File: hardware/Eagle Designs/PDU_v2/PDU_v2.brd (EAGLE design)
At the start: 160 x 100 mm, 277 parts, among them J1 5037630291, J10 5037630691, J11 2PIN_HEADER, J12 2PIN_HEADER, J13 5037630291, J14 5037630291, J15 2PIN_HEADER, J16 5037630291, J17 5037630291, J18 5037630291, J19 5037630291, J2 5037630291, J20 503182-1852, J21 5037630491, J22 UJ31-CH-G1-SMT-TR, J23 2PIN_HEADER, J24 2PIN_HEADER, J25 2PIN_HEADER, J26 1729128, J27 5037630491, J28 5037630491, J3 5037630291, J4 5037630291, J5 5037630291, J6 5037630291, J7 5037630491, J8 5037630491, J9 5037630491, M1 BSZ100N06LS3, M2 BSZ100N06LS3, M3 BSZ033NE2LS5, M4 BSZ033NE2LS5, SW1 KMR231GLFS, T1 2N5088, U1 DRV8847PWPR, U10 PE014006, U11 IRLML2803PBFCT-ND, U12 IRLML2803PBFCT-ND, U13 LT8390EFE#PBF, U14 ATSAME51N19A-AF, U15 INA219BIDR, U16 MAX706RESA+T, U17 MAX16998AAUA+T, U18 ADT7311WTRZ, U19 NTGD1100LT1G, U2 DRV8847PWPR, U20 AO3400, U21 LT8609A, U22 LT8609A, U23 LT8609A, U3 LTC1477CS8LINEAR_TECHNOLOGY_L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, U4 LTC1477CS8LINEAR_TECHNOLOGY_L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, U5 LTC1477CS8LINEAR_TECHNOLOGY_L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, U6 LTC1477CS8LINEAR_TECHNOLOGY_L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, U7 LTC1477CS8LINEAR_TECHNOLOGY_L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, U8 LT8609A, U9 LTC1477CS8LINEAR_TECHNOLOGY_L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, Y1 ABS07-32.768KHZ-T

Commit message: updated PDU v2 (pre-routing)
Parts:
- removed C94: 1 uF, HSFL_Main_Library:0805
- removed C95, C97: 10 uF, HSFL_Main_Library:0805
- removed C96: 0.1 uF, HSFL_Main_Library:0805
- removed C98: 4.7 uF, HSFL_Main_Library:0805
- removed J11, J12, J15, J23, J24, J25: 2PIN_HEADER, HSFL_Main_Library:2MM_2PIN_HEADER
- removed R82: 10k, HSFL_Main_Library:0805
- removed R83: 40.2, HSFL_Main_Library:0805
- removed R86, R87, R90: 1k, HSFL_Main_Library:0805
- removed R88: 2.2 uH, Artemis:RESC0805X60N
- removed R89: 100, HSFL_Main_Library:0805
- removed T1: 2N5088, Artemis:TO92
- removed U$3, U$5: NDS8434, Artemis:SO08
- added J29: 61300411021, Artemis:CONN_61300411021_WRE
- added L7: 2.2 uH, Artemis:IND_BOURNS_SRP7030
- added Q1, Q2: FDS6375, Artemis:SOIC127P600X175-8N
- added R41: 84.5k, HSFL_Main_Library:0603-RES
- C24, C36: device HSFL_Main_Library:0805 -> HSFL_Main_Library:1210
- C30, C38, C54, C55, C56, C57, C58, C59, C60, C61, C62, C63, C64, C65, C66, C67, C68, C70, C71, C91: device HSFL_Main_Library:0805 -> HSFL_Main_Library:0603-CAP
- C37: value 10 nF -> 22 uF; device HSFL_Main_Library:0805 -> HSFL_Main_Library:0603-CAP
- C39: value 0.1 uF -> 33 pF; device HSFL_Main_Library:0805 -> HSFL_Main_Library:0603-CAP
- C40: value 4.7 uF -> 0.1 uF; device HSFL_Main_Library:0805 -> HSFL_Main_Library:0603-CAP
- C41: value 10 pF -> 1 uF; device HSFL_Main_Library:0805 -> HSFL_Main_Library:0603-CAP
- C42: value 22 uF -> 4.7 uF; device HSFL_Main_Library:1206 -> HSFL_Main_Library:0603-CAP
- C5: value 10 nF -> 0.01 uF
- C69: value 44 uF -> 22 uF; device HSFL_Main_Library:0805 -> HSFL_Main_Library:0603-CAP
- C89: value 4.7 uF -> 10 uF; device HSFL_Main_Library:0805 -> HSFL_Main_Library:0603-CAP
- C90: value 1 uF -> 4.7 uF; device HSFL_Main_Library:0805 -> HSFL_Main_Library:0603-CAP
- C92: value 33 pF -> 10 uF; device HSFL_Main_Library:0805 -> HSFL_Main_Library:0603-CAP
- C93: value 0 uF -> 1 uF; device HSFL_Main_Library:0805 -> HSFL_Main_Library:0603-CAP
- J18, J19: value 5037630291 -> 5037630491; device Artemis:CON_5037630291 -> Artemis:CON_5037630491
- J22: value UJ31-CH-G1-SMT-TR -> UJ31-CH-314-SMT-TR; device Artemis:CUI_UJ31-CH-G1-SMT-TR -> Artemis:CUI_UJ31-CH-314-SMT-TR
- J27, J28: value 5037630491 -> 5037630691; device Artemis:CON_5037630491 -> Artemis:CONN_503763-0691_MOL
- L1, L3: device Artemis:IND_XFL4020-222ME -> Artemis:IND_BOURNS_SRP7030
- L2: value 1 uH -> 1 uH; device HSFL_Main_Library:ELL4GG -> Artemis:INDC1608X95N
- L4: value 2.2 uH -> 10 uH; device Artemis:IND_XFL4020-222ME -> Artemis:INDC2012X100N
- L6: value 10uH -> 2.2 uH; device HSFL_Main_Library:XFL4030472MEB -> Artemis:IND_BOURNS_SRP7030
- NT1, NT2, NT3: value 0 H -> AIMC-0805-2N2S-T; device HSFL_Main_Library:ELL4GG -> Artemis:INDC2012X105N
- R15: value 300k -> 301k
- R16, R24: value 49.9k -> 47k
- R23: value 182k -> 180k
- R26: value 18.2 K -> 1k; device HSFL_Main_Library:0805 -> HSFL_Main_Library:0603-RES
- R27: value 187 K -> 100; device HSFL_Main_Library:0805 -> HSFL_Main_Library:0603-RES
- R28: value 100 K -> 10k; device HSFL_Main_Library:0805 -> HSFL_Main_Library:0603-RES
- R29: value 1 M -> 40.2k; device HSFL_Main_Library:0805 -> HSFL_Main_Library:0603-RES
- R37: value 10 uH -> 2k; device Artemis:RESC0805X60N -> HSFL_Main_Library:0603-RES
- R38, R39, R40, R42, R45, R48, R49, R50, R51, R52, R53, R54, R55, R56, R64, R67, R72, R73, R74, R75, R76, R77, R78: device HSFL_Main_Library:0805 -> HSFL_Main_Library:0603-RES
- R59: value 80k -> 100k
- R60: value 50k -> 62k
- R63: value 125k -> 130k
- R65: value 191k -> 180k
- R66: value 9k -> 9.09k; device HSFL_Main_Library:0805 -> HSFL_Main_Library:0603-RES
- R79: value 71.5k -> 68.1k; device HSFL_Main_Library:0805 -> HSFL_Main_Library:0603-RES
- R80: value 86.6k -> 1k; device HSFL_Main_Library:0805 -> HSFL_Main_Library:0603-RES
- R81: value 2k -> 1k; device HSFL_Main_Library:0805 -> HSFL_Main_Library:0603-RES
- U20: value AO3400 -> AO3404A
- U23: value LT8609A -> BC848ALT1G; device HSFL_Main_Library:MSOP-10_MSE -> Artemis:SOT-23_ONS
- Y1: value ABS07-32.768KHZ-T -> CC4V-T1A-32.768KHZ-12.5PF-20PPM-TA-QC; device Artemis:XTAL_ABS07-32.768KHZ-T -> Artemis:XTAL_CC4V-T1A-32.768KHZ-12.5PF-20PPM-TA-QC
- moved R45 618.4 mm to (-520.7, -193.0)
- moved R50 596.1 mm to (-516.9, -193.0)
- moved L6 595.4 mm to (-518.2, -218.4)
- moved R51 586.5 mm to (-509.3, -193.0)
- moved R52 585.6 mm to (-513.1, -193.0)
- moved C30 582.3 mm to (-501.6, -193.0)
- moved R53 576.1 mm to (-505.5, -193.0)
- moved C66 574.1 mm to (-496.6, -193.0)
- moved C68 562.7 mm to (-491.5, -193.0)
- moved C67 555.3 mm to (-476.2, -193.0)
- moved C69 551.6 mm to (-481.3, -193.0)
- moved C37 548.1 mm to (-486.4, -193.0)
- moved C70 540.6 mm to (-471.2, -193.0)
- moved R57 531.0 mm to (-466.1, -189.2)
- moved R58 530.3 mm to (-466.1, -193.0)
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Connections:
- removed net 5V_BURN_RELAY: U14.54
- removed net BURNWIREHERE________________________: H1.2.8
- removed net N$33: C38.1, U23.3
- removed net N$34: C39.1, U23.1
- removed net N$35: C39.2, L4.1, U23.2
- removed net N$36: C41.1, R27.2, R29.1, U23.6
- removed net N$72: CR1.2, J11.1
- removed net N$73: CR2.2, J12.1
- removed net N$74: R89.2, R90.2, U20.3
- removed net N$75: CR3.2, J15.1
- removed net N$78: CR4.2, J23.1
- removed net N$79: CR5.2, J24.1
- removed net N$80: CR6.2, J25.1
- removed net N$98: NT1.P$2, R89.1, U$1.12
- removed net PG_5V_BURN: R28.1, U23.8
- removed net SOLAR_VS: C29.1, R34.1, R36.1, U15.5
- removed net SW_5V_BURN: C41.2, C42.1, L4.2, R28.2, R29.2
- removed net SW_5V_BURN_EN: U23.10
- removed net UART_TXD: H1.1.2
- new net BUS_3V1: L3.1
- new net N$20: L3.2
- net +3V3: now also R54.2, R58.2; no longer R54.1, R58.1
- net 12V_SW1: now also J10.5, L6.1; no longer J10.3, L6.2
- net 5V_BURN: now also H1.2.8, U14.54, U23.1; no longer T1.2
- net BATT_CHRG: now also C92.2, C93.2, J29.4; no longer C94.2, C95.2
- net BATT_CHRG_DISP: now also R40.2; no longer R40.1
- net BC_VCC: now also R37.1; no longer R81.1
- net BUS_3V3: now also C29.1, L1.1, R34.1, R36.1, U15.5; no longer L1.2
- net BUS_5V: no longer L3.2
- net GND: now also C37.1, C42.1, C69.1, C72.1, C90.1, C92.1, C93.1, J10.2, J18.2, J18.5, J18.6, J19.2, J19.5, J19.6, J22.SH10, J22.SH7, J22.SH8, J22.SH9, J27.2, J27.4, J28.2, J9.2, NT1.1, NT2.1, NT3.1, R40.1, U23.2; no longer C37.2, C38.2, C40.2, C42.2, C56.1, C57.1, C58.1, C59.1, C60.1, C69.2, C72.2, C94.1, C95.1, C97.1, C98.1, J10.5, J11.2, J12.2, J15.2, J18.3, J19.3, J23.2, J24.2, J25.2, J27.5, J28.5, J28.6, J9.3, NT1.P$1, NT2.P$1, NT3.P$1, R27.1, R38.1, R40.2, R90.1, T1.3, U14.12, U14.25, U14.30, U14.39, U14.51, U14.63, U14.77, U14.92, U23.11, U23.5
- net GNDA: now also C38.1, C39.1, C40.2, C41.2, NT1.2, NT2.2, R29.1, R41.2; no longer C90.2, C91.2, C92.1, C93.1, NT2.P$2, NT3.P$2, R83.1, R86.2
- net INH_SW1_COM: now also J18.3; no longer J18.2
- net INH_SW3_COM: now also J19.3; no longer J19.2
- net LX: now also L7.1; no longer R88.2
- net MID: now also NT3.2, R27.1, U$1.12
- net MOSI: now also J27.3; no longer J27.2
- net N$100: now also C91.2; no longer C96.2
- net N$12: now also L1.2; no longer L1.1
- net N$13: now also Q1.1, Q1.2, Q1.3, Q2.1, Q2.2, Q2.3; no longer U$3.1, U$3.2, U$3.3, U$5.1, U$5.2, U$5.3
- net N$15: now also Q2.4; no longer U$5.4
- net N$16: now also U23.3; no longer T1.1
- net N$18: now also Q1.4; no longer U$3.4
- net N$29: no longer L3.1
- net N$31: now also R27.2, U20.3; no longer U23.4
- net N$32: now also C56.1, C57.1, C58.1, C59.1, C60.1, R38.1, U14.12, U14.25, U14.30, U14.39, U14.51, U14.63, U14.77, U14.92; no longer C37.1, U23.7
- net N$43: now also L2.1; no longer L2.P$1
- net N$46: now also L4.2; no longer R37.2
- net N$51: now also L2.2; no longer L2.P$2
- net N$58: now also L4.1; no longer R37.1
- net N$66: now also C72.2; no longer C72.1
- net N$87: now also C41.1; no longer C90.1
- net N$89: now also R41.1; no longer R80.1
- net N$90: now also C40.1; no longer C91.1
- net N$92: now also R37.2; no longer R81.2
- net N$93: now also R28.2, R29.2; no longer R82.2, R83.2
- net N$95: now also C39.2, R28.1; no longer C92.2, R82.1
- net N$97: now also C38.2; no longer C93.2
- net N$99: now also R80.1, R81.1; no longer R86.1, R87.1
- net PB16: now also J28.3; no longer J28.1
- net PB17: now also J28.1; no longer J27.4
- net PB22: now also J28.6; no longer J28.3
- net PB23: now also J28.5; no longer J28.2
- net RESET: now also R58.1; no longer R58.2
- net SCK: now also J27.5; no longer J27.3
- net SOLAR_IN1: now also CR1.2, R35.1, U15.8
- net SOLAR_IN2: now also CR2.2
- net SOLAR_IN3: now also CR3.2
- net SOLAR_IN4: now also CR4.2
- net SOLAR_IN5: now also CR5.2
- net SOLAR_IN6: now also CR6.2
- net SW: now also C91.1, L7.2; no longer C96.1, R88.1
- net SWCLK: now also R54.1; no longer R54.2
- net SW_3V3_BUS: now also L6.2; no longer L6.1
- net SW_5V_1: now also J10.3; no longer J10.2
- net SW_5V_2: now also J26.1
- net SW_5V_3: now also J9.3; no longer J26.1, J9.2
- net UART2_TXD: now also H1.1.2
- net USB_JUMP1: now also C37.2, C69.2, J29.1; no longer C69.1
- net USB_JUMP_BAT: now also J29.3
- net VBATT: now also J29.2, R81.2; no longer C40.1, R35.1, R87.2, U15.8, U23.9
- net VBURN1: now also Q1.5, Q1.6, Q1.7, Q1.8; no longer U$3.5, U$3.6, U$3.7, U$3.8
- net VBURN2: now also Q2.5, Q2.6, Q2.7, Q2.8; no longer U$5.5, U$5.6, U$5.7, U$5.8
- net VL: now also C42.2, C90.2; no longer C97.2, C98.2

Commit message: updated PDU v2 and Artemis Library
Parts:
- removed D1: (no value), Artemis:POWERDI-123
- removed U10: PE014006, Artemis:RELAY5-PE_CO
- added Q3: AO4485, Artemis:SOIC127P600X175-8N
- added R86: 10k, HSFL_Main_Library:0603-RES
- Q1, Q2: device Artemis:SOIC127P600X175-8N -> Artemis:SOIC127P600X175-8N@1
- R36: device HSFL_Main_Library:0603-RES -> HSFL_Main_Library:0805
- moved R45 660.7 mm to (83.8, 73.7), flipped to the bottom, turned to 180 degrees
- moved R50 653.2 mm to (83.8, 63.5), flipped to the bottom, turned to 270 degrees
- moved R51 648.9 mm to (85.1, 67.3), flipped to the bottom
- moved R52 647.4 mm to (81.3, 63.5), flipped to the bottom, turned to 90 degrees
- moved R53 638.0 mm to (78.7, 63.5), flipped to the bottom, turned to 90 degrees
- moved C30 632.2 mm to (76.2, 63.5), flipped to the bottom, turned to 270 degrees
- moved C66 625.3 mm to (73.7, 63.5), flipped to the bottom, turned to 270 degrees
- moved C68 615.9 mm to (67.3, 66.0), flipped to the bottom
- moved C70 613.4 mm to (80.0, 76.2), flipped to the bottom, turned to 90 degrees
- moved L6 613.2 mm to (44.5, 25.4), turned to 180 degrees
- moved C37 612.4 mm to (67.3, 68.6), flipped to the bottom, turned to 180 degrees
- moved L7 611.8 mm to (34.3, 63.5), turned to 270 degrees
- moved C67 610.0 mm to (71.1, 76.2), flipped to the bottom
- moved C69 608.9 mm to (67.3, 71.1), flipped to the bottom, turned to 180 degrees
- moved J29 602.8 mm to (14.0, 69.8), flipped to the bottom, turned to 90 degrees
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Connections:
- net N$100 renamed BST
- net N$31 renamed R26_R27
- net N$69 renamed BUS_EN_VIN
- net N$85 renamed ACOK
- net N$87 renamed BATT_CHRG_VCC
- net N$88 renamed ILIM
- net N$89 renamed ISET
- net N$90 renamed TMR
- net N$91 renamed CHGOK
- net N$93 renamed IB
- net N$94 renamed VNTC
- net N$95 renamed R28_C39
- net N$96 renamed NTC
- net N$97 renamed R85_C38
- net N$99 renamed FB
- removed net +3V3: C64.1, D2.3, J20.4, J21.1, R38.2, R42.2, R54.2, R55.2, R58.2, R60.2, R61.2, R62.2, U16.2
- removed net BUS_3V1: L3.1
- removed net N$20: L3.2
- net BUS_3V3: now also C64.1, D2.3, J20.4, J21.1, R38.2, R42.2, R54.2, R55.2, R58.2, R60.2, R61.2, R62.2, U16.2
- net BUS_5V: now also L3.1
- net GND: no longer U10.12
- net N$13: now also Q3.5, Q3.6, Q3.7, Q3.8; no longer U10.11
- net N$16: now also Q3.4, R86.1; no longer D1.A, U10.5
- net N$29: now also L3.2
- net PB16: now also J28.1; no longer J28.3
- net PB17: now also J28.3; no longer J28.1
- net PB22: now also J28.5; no longer J28.6
- net PB23: now also J28.6; no longer J28.5
- net VBATT: now also Q3.1, Q3.2, Q3.3, R86.2; no longer D1.C, U10.1, U10.14
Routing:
- net N$32: track 0.00 -> 50.3 mm, vias 0 -> 3
- net N$13: track 0.00 -> 45.5 mm, vias 0 -> 2
- net N$18: track 0.00 -> 33.8 mm
- net PB23: track 0.00 -> 29.0 mm
- net PB22: track 0.00 -> 28.8 mm
- net PB16: track 0.00 -> 28.6 mm
- net GND: track 0.00 -> 28.3 mm
- net PB17: track 0.00 -> 28.3 mm
- net VBURN2: track 0.00 -> 22.5 mm
- net WDT_WDI: track 0.00 -> 20.6 mm
- net VBURN1: track 0.00 -> 20.3 mm
- net N$23: track 0.00 -> 19.2 mm, vias 0 -> 2
- net N$21: track 0.00 -> 19.2 mm, vias 0 -> 2
- net N$54: track 0.00 -> 18.3 mm
- net VBATT: track 0.00 -> 18.2 mm, vias 0 -> 1
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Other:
- board size 160 x 100 mm -> 90.2 x 95.5 mm

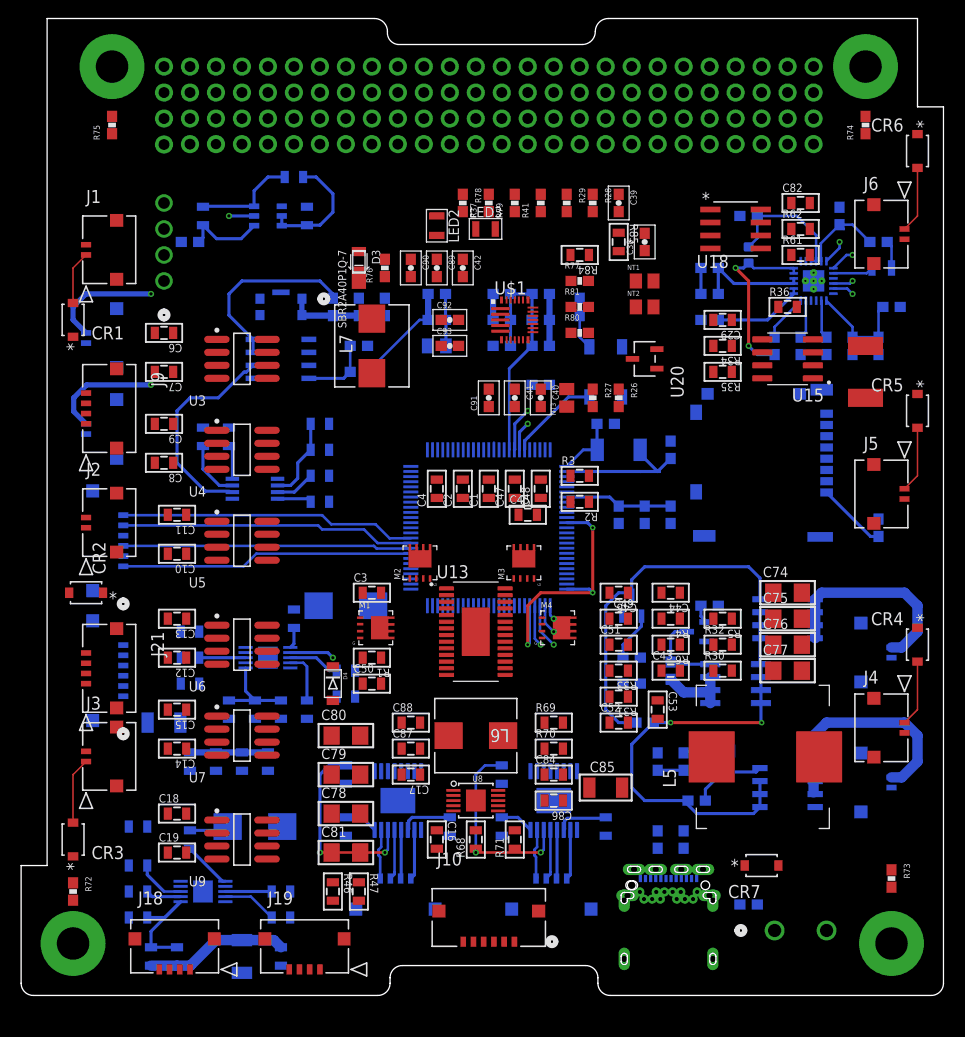
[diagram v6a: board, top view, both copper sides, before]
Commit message: updated PDU v2 (Routing Rough Draft complete)
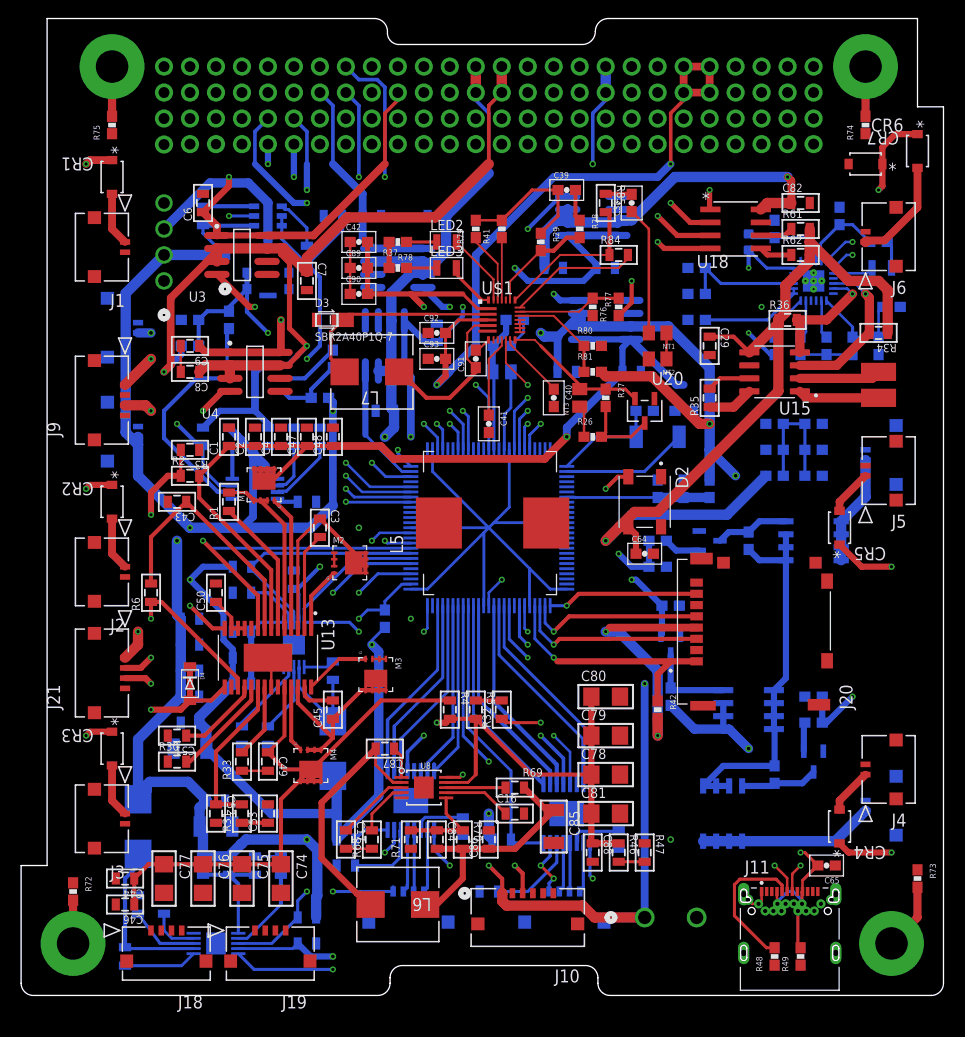
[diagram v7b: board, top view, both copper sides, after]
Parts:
- removed J22: UJ31-CH-314-SMT-TR, Artemis:CUI_UJ31-CH-314-SMT-TR
- removed J27, J28: 5037630691, Artemis:CONN_503763-0691_MOL
- added J11: UJ31-CH-G1-SMT-TR, Artemis:CUI_UJ31-CH-G1-SMT-TR
- moved CR7 69.3 mm to (82.5, 81.3), turned to 180 degrees
- moved C19 64.7 mm to (59.7, 61.0), flipped to the bottom, turned to 180 degrees
- moved C77 64.3 mm to (14.0, 11.4), turned to 270 degrees
- moved U9 62.0 mm to (57.1, 66.0), flipped to the bottom, turned to 180 degrees
- moved C76 61.6 mm to (17.8, 11.4), turned to 270 degrees
- moved U7 61.3 mm to (55.9, 76.2), flipped to the bottom, turned to 180 degrees
- moved C44 60.2 mm to (10.2, 11.4)
- moved C15 60.2 mm to (57.1, 71.1), flipped to the bottom
- moved C14 59.7 mm to (52.1, 71.1), flipped to the bottom
- moved C75 59.1 mm to (21.6, 11.4), turned to 270 degrees
- moved C18 57.6 mm to (53.3, 61.0), flipped to the bottom, turned to 180 degrees
- moved C46 57.1 mm to (10.2, 8.89)
- moved C74 56.9 mm to (25.4, 11.4), turned to 270 degrees
- moved R30 54.1 mm to (15.2, 22.9)
- moved R6 51.1 mm to (12.7, 39.4), turned to 90 degrees
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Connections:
- net N$32 renamed VDD
- removed net +3V3_BUS: R43.1, R44.1
- removed net +5V_BUS: C25.2, C26.2, C27.2, C28.2, U1.12, U2.12
- removed net MISO: J27.1, U14.48
- removed net MOSI: J27.3, U14.46
- removed net N$42: U13.23
- removed net N$65: D2.2, U14.95
- removed net PB16: J28.1, U14.58
- removed net PB17: J28.3, U14.59
- removed net PB22: J28.5, U14.60
- removed net PB23: J28.6, U14.61
- removed net PDU_RX: H1.1.51, U14.83
- removed net PDU_TX: H1.1.49, U14.82
- removed net SCK: J27.5, U14.47
- new net LED: D2.2, U14.73
- new net N$20: H1.1.32
- net 5V_BURN: now also U14.82; no longer H1.2.8, U14.54
- net 5V_USB_CHRG: no longer H1.1.32
- net BURN1_EN: now also U14.83; no longer U14.55
- net BURN2_EN: now also U14.84; no longer U14.70
- net BUS_3V3: now also R43.1, R44.1
- net BUS_3V3_PG: now also U14.58; no longer U14.71
- net BUS_5V: now also C25.2, C26.2, C27.2, C28.2, U1.12, U2.12
- net BUS_5V_PG: now also U14.56; no longer U14.75
- net BUS_EN: now also U14.57; no longer U14.74
- net CUS_SCL: now also U14.93; no longer U14.73
- net CUS_SDA: now also U14.94; no longer U14.72
- net FAULT1: now also U14.42; no longer H1.1.40, U14.65
- net FAULT2: no longer H1.1.46, U14.80
- net GND: now also J11.A1, J11.A12, J11.B1, J11.B12, J11.SH1, J11.SH2, J11.SH3, J11.SH4, J11.SH5, J11.SH6; no longer J22.A1, J22.A12, J22.B1, J22.B12, J22.SH1, J22.SH10, J22.SH2, J22.SH3, J22.SH4, J22.SH5, J22.SH6, J22.SH7, J22.SH8, J22.SH9, J27.2, J27.4, J27.6, J28.2, J28.4
- net IN1: now also U14.35; no longer H1.1.24, U14.34
- net IN2: now also U14.36; no longer H1.1.23, U14.35
- net IN3: now also U14.41; no longer H1.1.25, U14.36
- net IN4: now also U14.40; no longer H1.1.26, U14.37
- net IN5: now also U14.44; no longer H1.1.28, U14.67
- net IN6: now also U14.45; no longer H1.1.27, U14.68
- net IN7: now also U14.48; no longer H1.1.29, U14.69
- net IN8: now also U14.47; no longer H1.1.30, U14.78
- net SD_CS: now also U14.29; no longer U14.28
- net SD_MISO: now also U14.26; no longer U14.29
- net SD_MOSI: now also U14.28; no longer U14.26
- net SLEEP1: now also U14.34; no longer H1.1.42, U14.64
- net SLEEP2: now also U14.43; no longer H1.1.48, U14.79
- net SWCLK: now also U14.52; no longer U14.93
- net SWDIO: now also U14.54; no longer U14.94
- net SW_12V_EN1: now also U14.59; no longer U14.40
- net SW_12V_PGOOD: now also U14.60; no longer U14.41
- net SW_3V3_EN1: now also U14.71; no longer U14.42
- net SW_3V3_EN2: now also U14.70; no longer U14.43
- net SW_5V_EN1: now also U14.75; no longer U14.44
- net SW_5V_EN2: now also U14.74; no longer U14.45
- net SW_5V_EN3: now also U14.78; no longer U14.56
- net SW_VBATT_EN1: now also U14.79; no longer U14.57
- net TRQ1: now also U14.37; no longer H1.1.38, U14.66
- net TRQ2: now also U14.46; no longer H1.1.44, U14.81
- net UART2_RXD: now also U14.69; no longer U14.52
- net UART2_TXD: now also U14.68; no longer U14.53
- net USB_CC1: now also J11.A5; no longer J22.A5
- net USB_CC2: now also J11.B5; no longer J22.B5
- net USB_D+: now also J11.A6, J11.B6, U14.95; no longer J22.A6, J22.B6, U14.85
- net USB_D-: now also J11.A7, J11.B7, U14.96; no longer J22.A7, J22.B7, U14.84
- net USB_VBUS: now also J11.A4, J11.A9, J11.B4, J11.B9; no longer J22.A4, J22.A9, J22.B4, J22.B9
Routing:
- net VBATT: track 18.2 -> 426.0 mm, vias 1 -> 10
- net BUS_3V3: track 3.44 -> 371.8 mm, vias 0 -> 9
- net VL: track 0.00 -> 298.8 mm, vias 0 -> 8
- net BUS_5V: track 14.0 -> 250.2 mm, vias 0 -> 7
- net BUS_VBATT: track 0.00 -> 155.1 mm, vias 0 -> 1
- net BATT_CHRG: track 11.2 -> 158.3 mm, vias 1 -> 3
- net SW_5V_2: track 0.00 -> 130.6 mm, vias 0 -> 6
- net RESET: track 15.4 -> 139.2 mm, vias 1 -> 4
- net USB_D+: track 2.41 -> 121.0 mm, vias 1 -> 3
- net USB_D-: track 2.44 -> 113.9 mm, vias 1 -> 3
- net SW_5V_1: track 0.00 -> 108.8 mm, vias 0 -> 1
- net BUS_EN: track 11.9 -> 114.4 mm, vias 0 -> 3
- net SW_5V_3: track 0.00 -> 99.5 mm, vias 0 -> 3
- net CUS_SDA: track 1.98 -> 87.3 mm, vias 1 -> 3
- net 12V_OUT: track 0.00 -> 83.5 mm, vias 0 -> 2
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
